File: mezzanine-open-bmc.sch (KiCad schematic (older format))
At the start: 45 parts, among them P1 CONN_02X20, P2 CONN_02X20, Q1 S8050, Q2 S8050, SW1 PWR, SW2 RST, U1 FT230XS, U2 LM3940, U3 DS3231N, U4 PCA9306

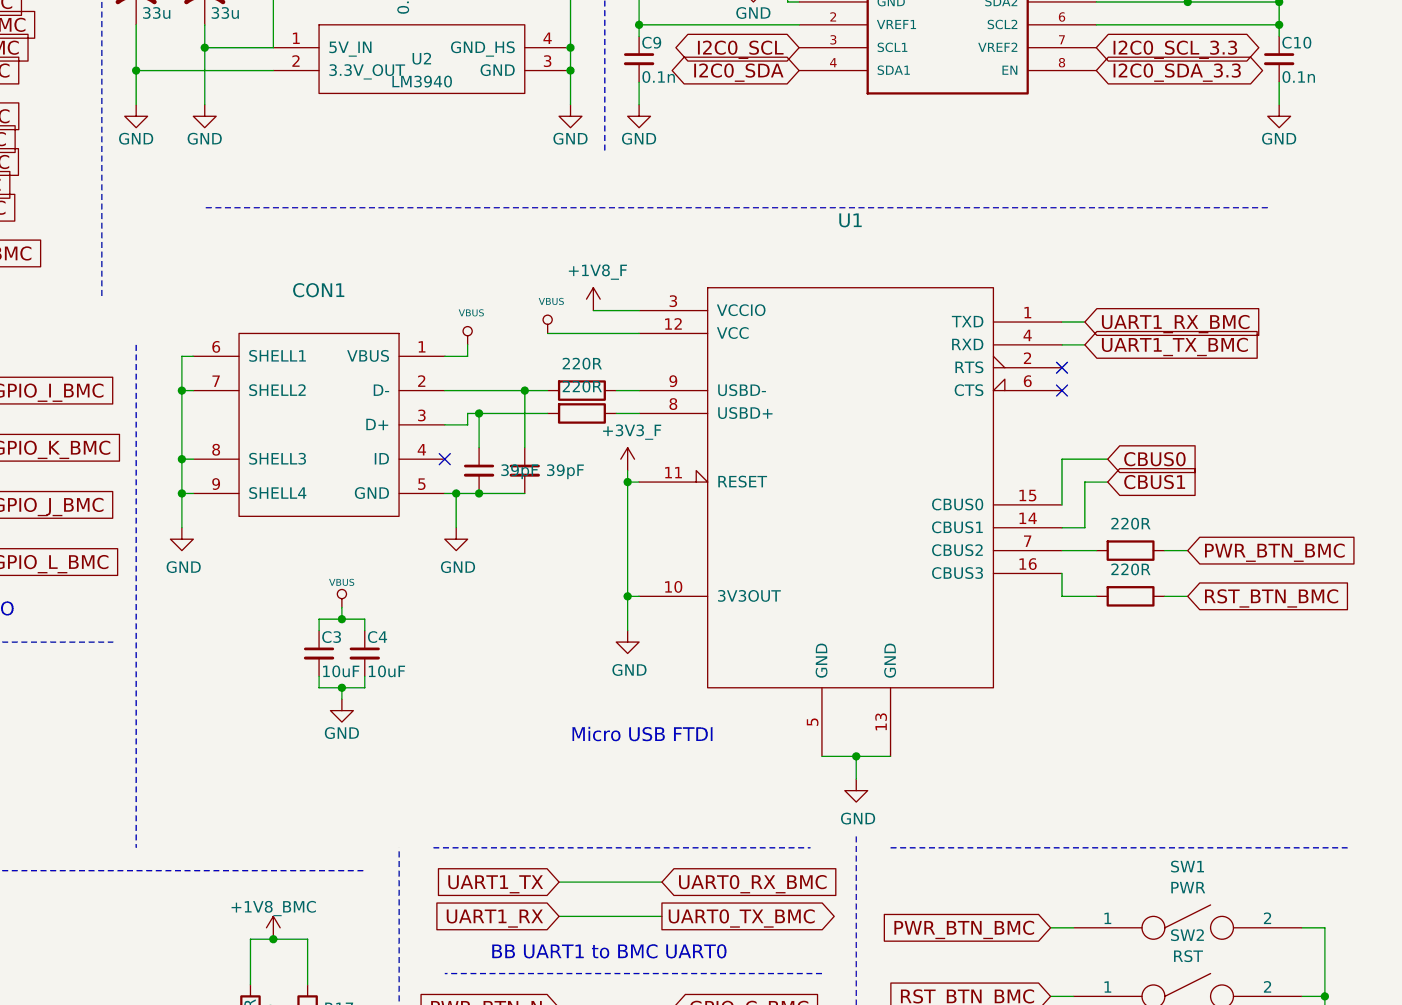
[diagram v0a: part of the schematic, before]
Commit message: Remove PWR from FT230XS Pin 10, Add Capacitor
Pin 10 already gets power from LDO, so additional 3v3
power has been removed.

Capacitor has been added for safety :)

Decoupling caps has been moved closer to the VBUS signals
to show they need  to be close together.

Signed-off-by: Sophie Haynes <sophie.haynes@linaro.org>
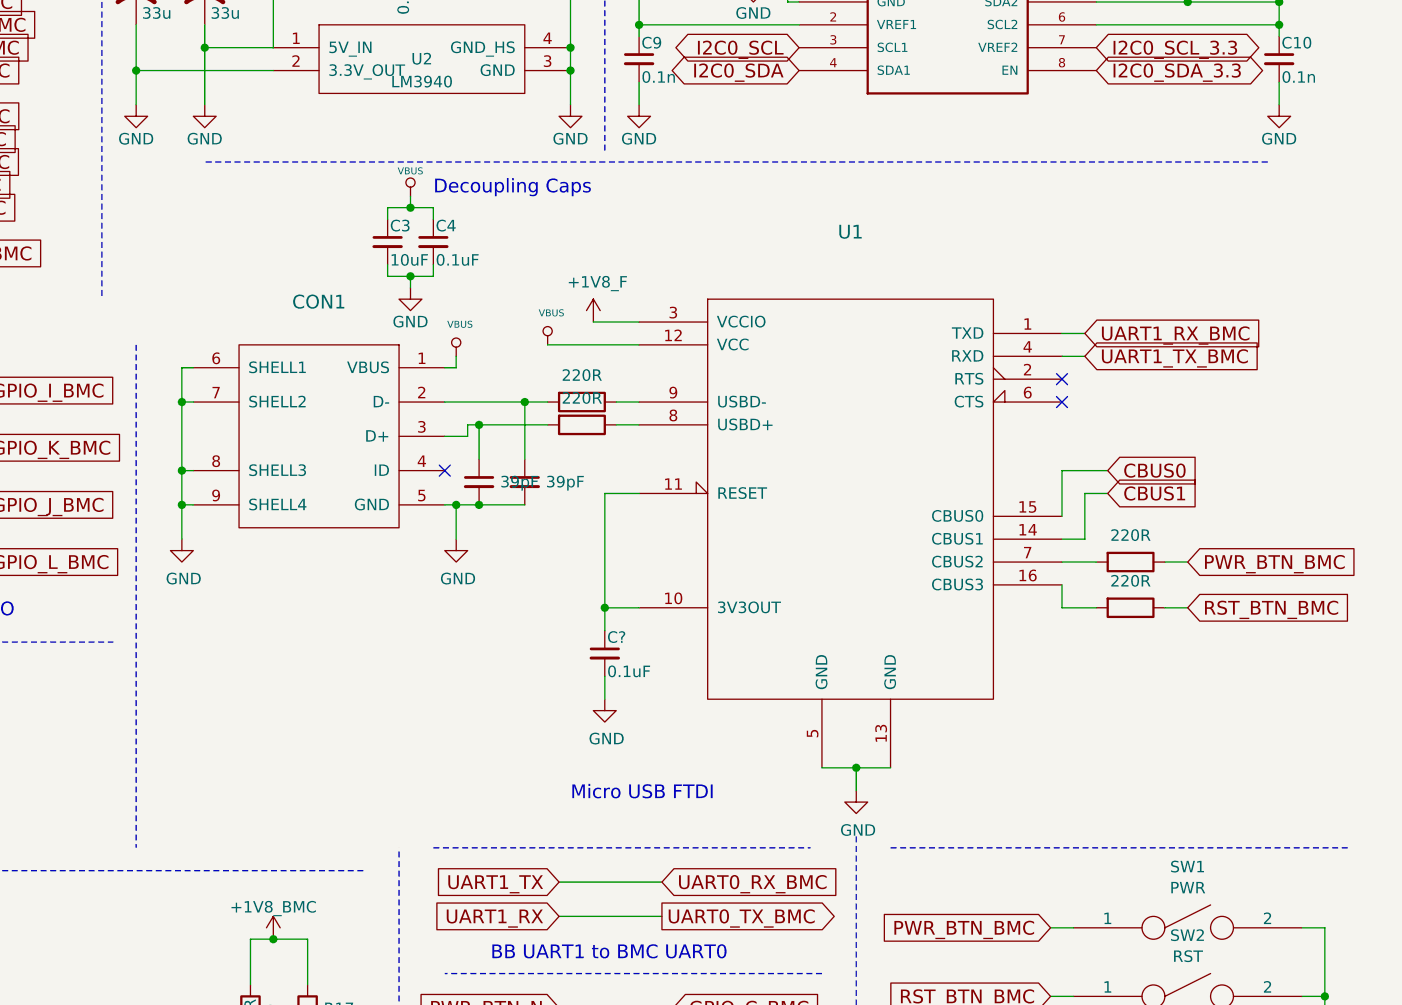
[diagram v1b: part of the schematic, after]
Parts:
- added C?: 0.1uF, Capacitors_SMD:C_0603, symbol C_Small
- C4: value 10uF -> 0.1uF
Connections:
- net +3V3_F renamed GND
- net GND: now also C?.2; no longer U1.10 (3V3OUT), U1.11 (RESET)
- new net: C?.1, U1.10 (3V3OUT), U1.11 (RESET)
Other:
- note added: "Decoupling Caps"
- moved on the sheet: C3, C4, CON1, U1

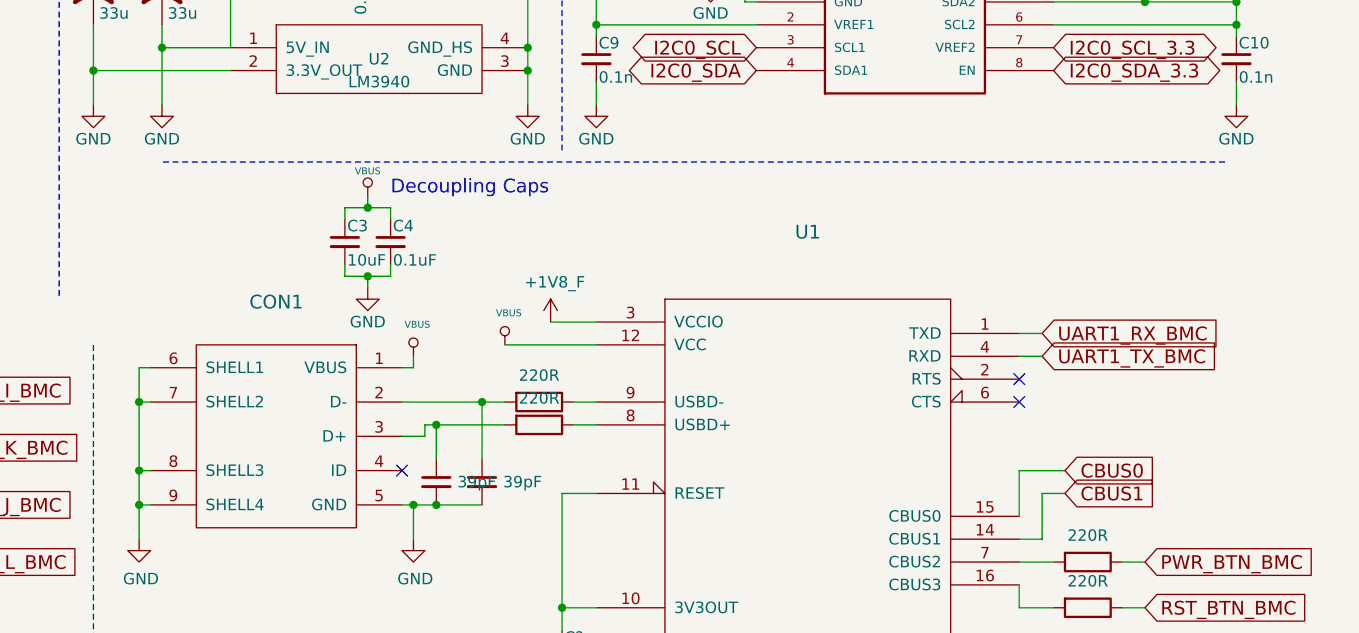
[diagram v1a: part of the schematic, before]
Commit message: Pull Down CTS on FT230XS
So that this pin is not "floating", it has been pulled down with a
10KΩ resistor.

Signed-off-by: Sophie Haynes <sophie.haynes@linaro.org>
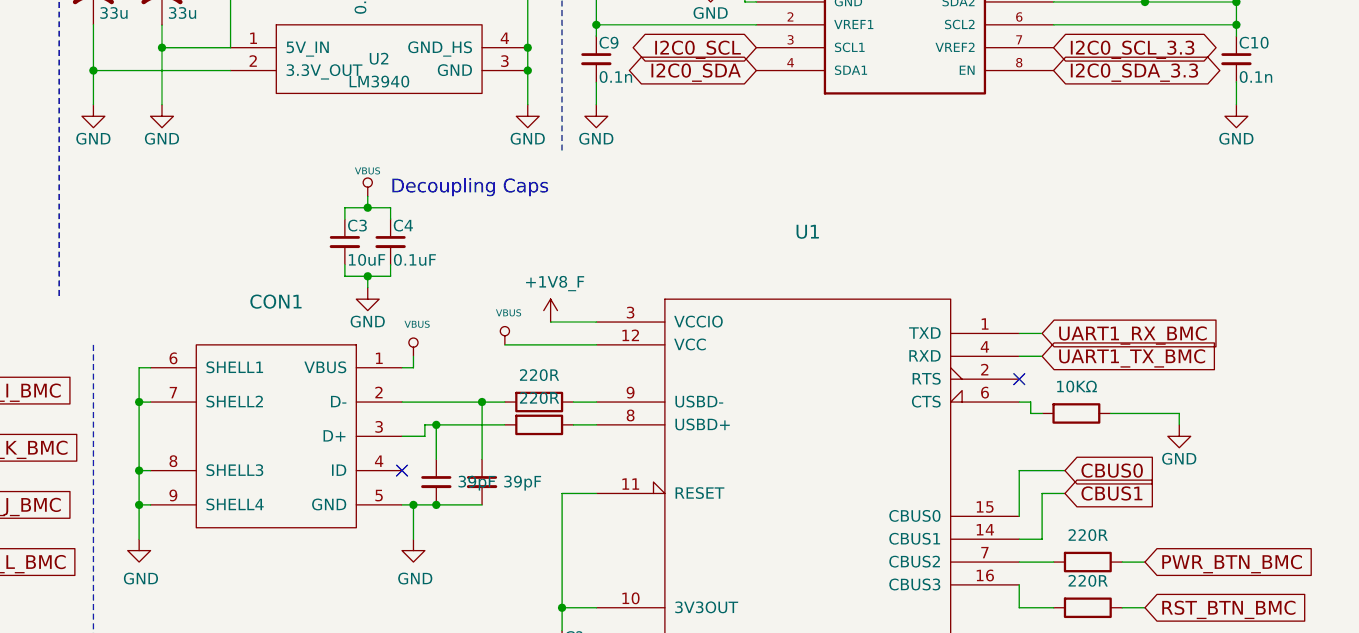
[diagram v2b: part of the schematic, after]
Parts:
- added R?: 10KΩ, Resistors_SMD:R_0603, symbol 220R
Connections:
- net GND: now also R?.1
- net at U1.6 (CTS): now also R?.2
- no-connect marks 6 -> 5

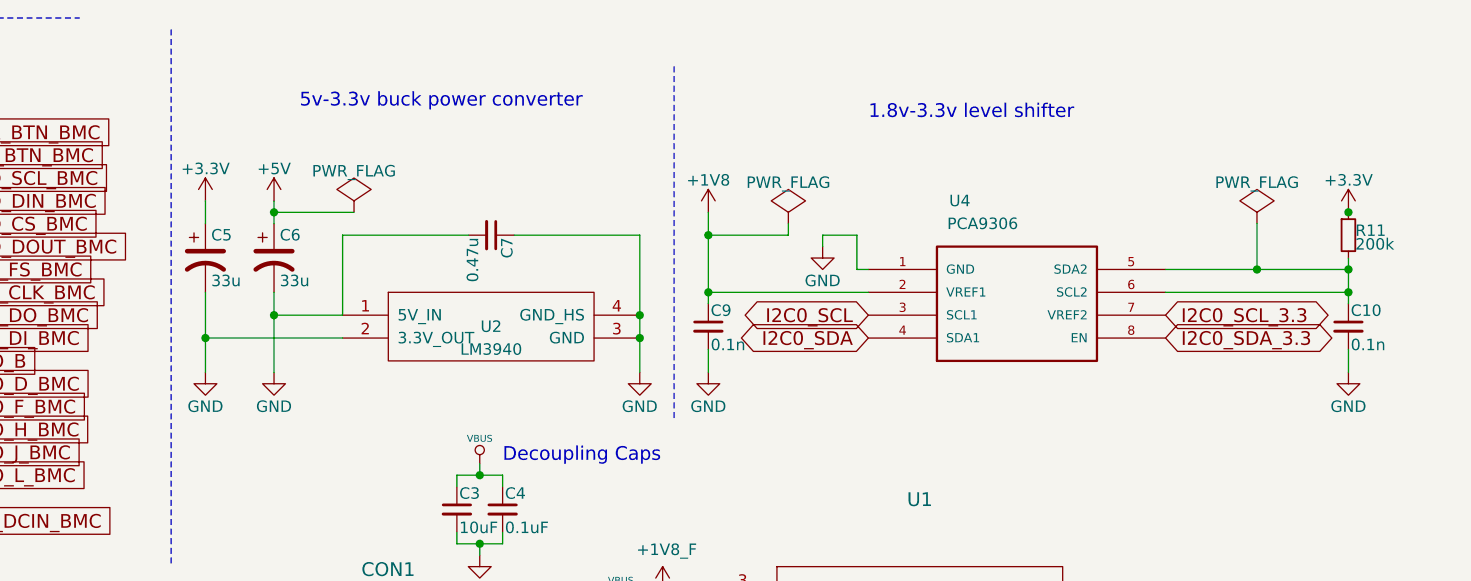
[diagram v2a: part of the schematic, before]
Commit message: Add Resistors to I2C0_SCL/SDA_3.3
Acting as pull up registers

Signed-off-by: Sophie Haynes<sophie.haynes@linaro.org>
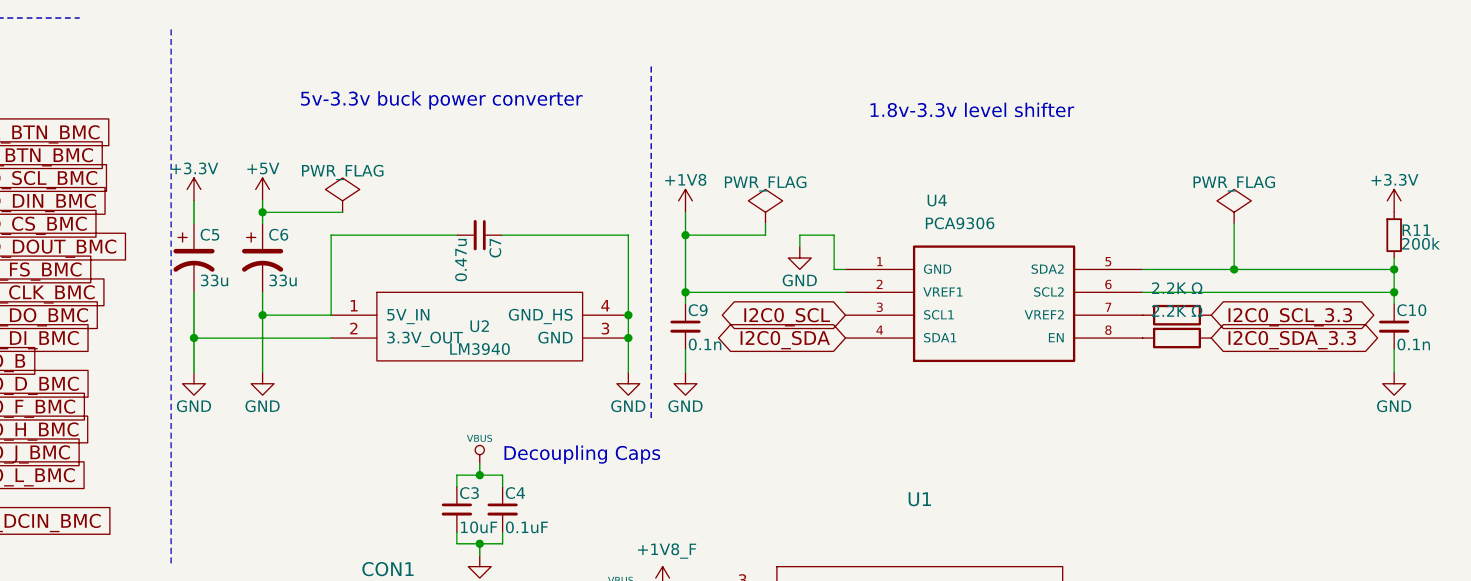
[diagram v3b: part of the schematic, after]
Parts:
- added R? (x2): 2.2K Ω, Resistors_SMD:R_0603, symbol 220R
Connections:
- net I2C0_SCL_3.3: now also R?.1; no longer U4.7 (VREF2)
- net I2C0_SDA_3.3: now also R?.1; no longer U4.8 (EN)
- new net: R?.2, U4.7 (VREF2)
- new net: R?.2, U4.8 (EN)
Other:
- moved on the sheet: C10, C5, C6, C7, C9, R11, U2, U4

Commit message: Change PWR Converter & Fix Library Issues/Confusing Jiggery Pokery
This commit attempts to fix loading issues with libraries
and footprints. The correct footprint for SOT-233 has been applied
to the 5v-3v3 buck power converted and has been tweaked as needed.
Signed-off-by: Sophie Haynes <sophie.haynes@linaro.org>
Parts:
- removed C6: 33u, symbol CP1
- removed C7: 0.47u, Capacitors_SMD:C_0603, symbol C_Small
- removed U2: LM3940, symbol LM3940
- added C6: 0.47u, Capacitors_SMD:C_0603, symbol C_Small
- added C7: 33u, symbol CP1
- added U2: PMIC-CJT1117-3.3(SOT223), 96boards:SOT-223, symbol PMIC-CJT1117-3.3(SOT223)
- gave numbers to parts that had none: 4
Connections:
- wire segments 233 -> 232

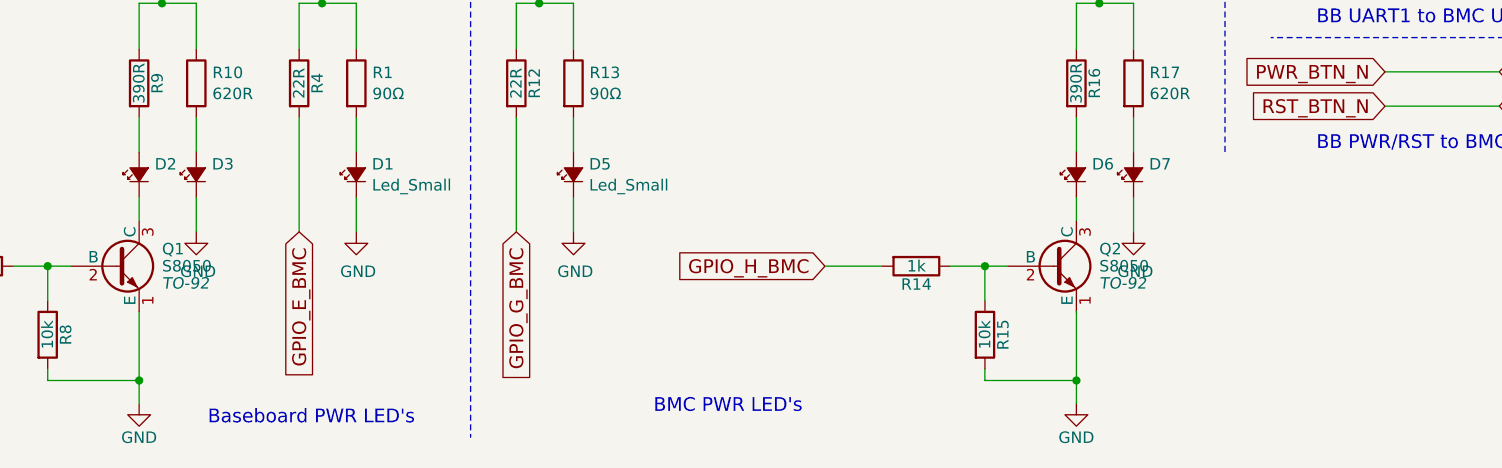
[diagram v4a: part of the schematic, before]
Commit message: Add New Footprints and Assign to Transistors
Footprints have been added to the .pretty folder.
Footprint for the transistors Q1 & Q2 have been assigned.

Signed-off-by: Sophie Haynes <sophie.haynes@linaro.org>
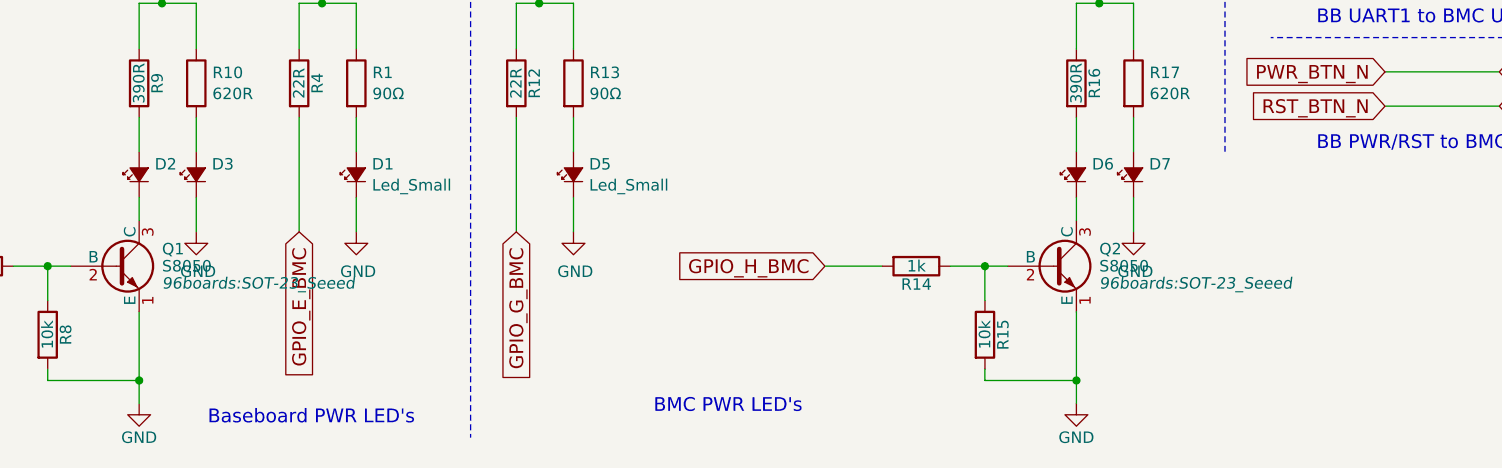
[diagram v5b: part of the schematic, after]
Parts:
- Q1, Q2: footprint TO-92 -> 96boards:SOT-23_Seeed

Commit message: Add EEPROM for I2C Lines to Schematic
First attempt at connecting i2c lines to EEPROM. Currently only connected to
the BMC pins. This will be changed so it is also connected to the baseboard
i2c

Signed-off-by: Sophie Haynes <sophie.haynes@linaro.org>
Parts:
- added U?: M24C16-WMN6P, SOIC127P600X175-8N, symbol M24C16-WMN6P
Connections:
- net labels added: +3V3
- wire segments 232 -> 241
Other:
- note added: "EEPROM for I2C0"

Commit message: Remove "_BMC" Suffix From I2C0 Lines
To improve i2c connections with the EEPROM, signal names
have been changed.

Signed-off-by: Sophie Haynes <sophie.haynes@linaro.org>
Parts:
- gave numbers to parts that had none: 1
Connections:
- net labels removed: I2C0_SCL_BMC, I2C0_SDA_BMC

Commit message: Create Correct Footprint for PCA9306, Assign Footprint, Connect U4
The PCA footprint was incorrect. This has been fixed; there are two
different models so both types have been added. It has been assigned
accordingly in the schematic.

U4(level shifter 1.8-3.3v) has been connected up.

Signed-off-by: Sophie Haynes <sophie.haynes@linaro.org>
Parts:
- U5: footprint SOIC127P600X175-8N -> 96boards:SOIC127P600X175-8N
